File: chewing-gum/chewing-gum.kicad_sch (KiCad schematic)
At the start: 19 parts, among them IC9 INA212AIDCKR, J15 Conn_02x01, J23 Conn_02x01, J28 Conn_01x03, J36 Conn_01x01_Socket, J42 Conn_Coaxial, J78 Conn_01x03, U21 TLV75801PDBV

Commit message: First version of the chewing gum Vdc
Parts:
- removed J36: Conn_01x01_Socket, Connector:Banana_Jack_1Pin, symbol Connector:Conn_01x01_Socket
- removed TPVBLD3: TestPoint, TestPoint:TestPoint_Plated_Hole_D2.0mm, symbol Connector:TestPoint
- added J10, J9: Conn_01x04, Connector_PinHeader_1.27mm:PinHeader_1x04_P1.27mm_Vertical, symbol Connector_Generic:Conn_01x04
- added J11: Conn_02x01, Connector_PinHeader_2.54mm:PinHeader_1x02_P2.54mm_Vertical, symbol Connector_Generic:Conn_02x01
- added J6: Conn_01x01_Socket, Connector:Banana_Jack_1Pin, symbol Connector:Conn_01x01_Socket
- added J7, J8: Conn_01x06, Connector_PinHeader_1.27mm:PinHeader_1x06_P1.27mm_Vertical, symbol Connector_Generic:Conn_01x06
- added R4: 48.7k, Resistor_SMD:R_0603_1608Metric, symbol Device:R_Small
- renumbered C57 to C1, C41 to C2, C58 to C3, IC9 to IC1, J28 to J1, J42 to J2, J78 to J3, J15 to J4, J23 to J5, R49 to R1, R34 to R2, R41 to R3, R42 to R5, R20 to R6, RV5 to RV1, U21 to U1
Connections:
- net 3V3_LDO is gone; now on net 3V3: J1.1 (Pin_1)
- net GND: now also J10.1 (Pin_1), J10.2 (Pin_2), J7.3 (Pin_3), J8.3 (Pin_3), J9.1 (Pin_1), J9.2 (Pin_2), R4.2
- net REF_INA: now also J8.6 (Pin_6)
- net V_ldo_feedback: now reaches J3.2 (Pin_2), R3.1, U1.4 (FB)
- net V_ldo_feedback: now also J7.1 (Pin_1)
- net +3.3VA renamed 3V3
- net 3V3: now also J8.5 (Pin_5)
- net DAC4 renamed DAC_ctrl
- net DAC_ctrl: now also J7.2 (Pin_2), R4.1
- net EN_VBLADE3 renamed LDO_EN_EXT
- net LDO_EN_EXT: now also J8.1 (Pin_1)
- net V_B3_INA renamed V_out_test_p
- net V_out_test_p: now also J11.2 (Pin_2)
- net V_B3_load renamed V_out
- net V_out: now also J6.1 (Pin_1), J9.3 (Pin_3), J9.4 (Pin_4)
- net V_B3_load_n renamed V_out_test_n
- net V_out_test_n: now also J11.1 (Pin_1)
- net V_B3_o renamed V_diff_ampl_out
- net V_diff_ampl_out: now also J10.3 (Pin_3)
- net vblade3_ldo renamed V_ldo_out
- net V_ldo_out: now also J7.6 (Pin_6)
- no-connect marks 1 -> 0
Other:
- note added: "1-2: LDO on 2-3: External enable open: LDO off"
- note added: "1-2: Trimmer Control 2-3: DAC Control"
- note removed: "1-2: LDO on 2-3: I2C enables LDO open: LDO off"
- note removed: "1-2: Potentiometer Control 2-3: DAC Control"
- moved on the sheet: C2, IC1, J1, J2, J3, J4, J5, R6

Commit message: Finished ADC/DAC board
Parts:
- removed J6: Conn_01x01_Socket, Connector:Banana_Jack_1Pin, symbol Connector:Conn_01x01_Socket
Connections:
- net GND: now also J8.4 (Pin_4); no longer J8.3 (Pin_3)
- net V_diff_ampl_out: now also J10.4 (Pin_4); no longer J10.3 (Pin_3)
- no-connect marks 0 -> 5
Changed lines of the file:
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@@
-	)
-	(junction
-		(at 142.24 55.88)
-		(diameter 0)
-		(color 0 0 0 0)
 	)
 	(junction
@@
 		(color 0 0 0 0)
 	)
+	(no_connect
+		(at 116.84 147.32)
+	)
+	(no_connect
+		(at 143.51 173.99)
+	)
+	(no_connect
+		(at 149.86 142.24)
+	)
+	(no_connect
+		(at 149.86 139.7)
+	)
+	(no_connect
+		(at 116.84 144.78)
+	)
 	(wire
 		(pts
@@
 	(wire
 		(pts
-			(xy 142.24 173.99) (xy 144.78 173.99)
-		)
-		(stroke
-			(width 0)
-			(type default)
-		)
-	)
-	(wire
-		(pts
 			(xy 49.53 81.28) (xy 49.53 83.82)
 		)
@@
 	(wire
 		(pts
-			(xy 142.24 53.34) (xy 142.24 55.88)
-		)
-		(stroke
-			(width 0)
-			(type default)
-		)
-	)
-	(wire
-		(pts
 			(xy 67.31 170.18) (xy 87.63 170.18)
 		)
@@
 	(wire
 		(pts
-			(xy 152.4 53.34) (xy 142.24 53.34)
-		)
-		(stroke
-			(width 0)
-			(type default)
-		)
-	)
-	(wire
-		(pts
 			(xy 110.49 168.91) (xy 110.49 170.18)
 		)
@@
 	(wire
 		(pts
+			(xy 143.51 173.99) (xy 144.78 173.99)
+		)
+		(stroke
+			(width 0)
+			(type default)
+		)
+	)
+	(wire
+		(pts
 			(xy 103.505 96.52) (xy 93.98 96.52)
 		)
@@
 		(pts
 			(xy 116.84 91.44) (xy 116.84 93.98)
+		)
+		(stroke
+			(width 0)
+			(type default)
+		)
+	)
+	(wire
+		(pts
+			(xy 143.51 176.53) (xy 144.78 176.53)
 		)
 		(stroke
@@
 		)
 	)
-	(label "GND"
-		(at 149.86 142.24 180)
-		(effects
-			(font
-				(size 1.27 1.27)
-			)
-			(justify right bottom)
-		)
-	)
 	(label "3V3"
 		(at 53.34 83.82 180)
@@
 	)
 	(label "V_diff_ampl_out"
-		(at 142.24 173.99 180)
+		(at 143.51 176.53 180)
 		(effects
 			(font
@@
 			)
 			(justify left bottom)
+		)
+	)
+	(label "GND"
+		(at 149.86 144.78 180)
+		(effects
+			(font
+				(size 1.27 1.27)
+			)
+			(justify right bottom)
 		)
 	)
@@
 					(unit 1)
 				)
-			)
-		)
-	)
-	(symbol
-		(lib_id "Connector:Conn_01x01_Socket")
-		(at 157.48 53.34 0)
-		(unit 1)
-		(exclude_from_sim no)
-		(in_bom yes)
-		(on_board yes)
-		(dnp no)
-		(property "Reference" "J6"
-			(at 157.48 57.15 90)
-			(effects
-				(font
-					(size 1.27 1.27)
-				)
-				(justify left)
-			)
-		)
-		(property "Value" "Conn_01x01_Socket"
-			(at 165.735 53.34 0)
-			(effects
-				(font
-					(size 1.27 1.27)
-				)
-				(justify left)
-				(hide yes)
-			)
-		)
-		(property "Footprint" "Connector:Banana_Jack_1Pin"
-			(at 157.48 53.34 0)
-			(effects
-				(font
-					(size 1.27 1.27)
-				)
-				(hide yes)
-			)
-		)
-		(property "Datasheet" "~"
-			(at 157.48 53.34 0)
-			(effects
-				(font
-					(size 1.27 1.27)
-				)
-				(hide yes)
-			)
-		)
-		(property "Description" ""
-			(at 157.48 53.34 0)
-			(effects
-				(font
-					(size 1.27 1.27)
-				)
-				(hide yes)
-			)
-		)
-		(pin "1"
-		)
-		(instances
-			(project "chewing-gum"
-				(path "/c199eb24-c33c-4d87-8bb8-b17a18fed446"
-					(reference "J6")
-					(unit 1)
-				)

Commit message: Before re-organizing the main board
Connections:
- net Vpm is gone; now on net 5V: C1.1, U1.1 (IN)
- net 5V: now reaches J8.2 (Pin_2)
- net 5V: now also J8.3 (Pin_3)
- no-connect marks 5 -> 3
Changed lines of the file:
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@@
-	)
-	(no_connect
-		(at 149.86 142.24)
-	)
-	(no_connect
-		(at 149.86 139.7)
 	)
 	(no_connect
@@
 		)
 	)
+	(label "5V"
+		(at 149.86 139.7 180)
+		(effects
+			(font
+				(size 1.27 1.27)
+			)
+			(justify right bottom)
+		)
+	)
 	(label "V_diff_ampl_out"
 		(at 68.58 170.18 0)
@@
 		)
 	)
-	(label "Vpm"
+	(label "5V"
 		(at 33.02 91.44 0)
 		(effects
@@
 		)
 	)
+	(label "5V"
+		(at 149.86 142.24 180)
+		(effects
+			(font
+				(size 1.27 1.27)
+			)
+			(justify right bottom)
+		)
+	)

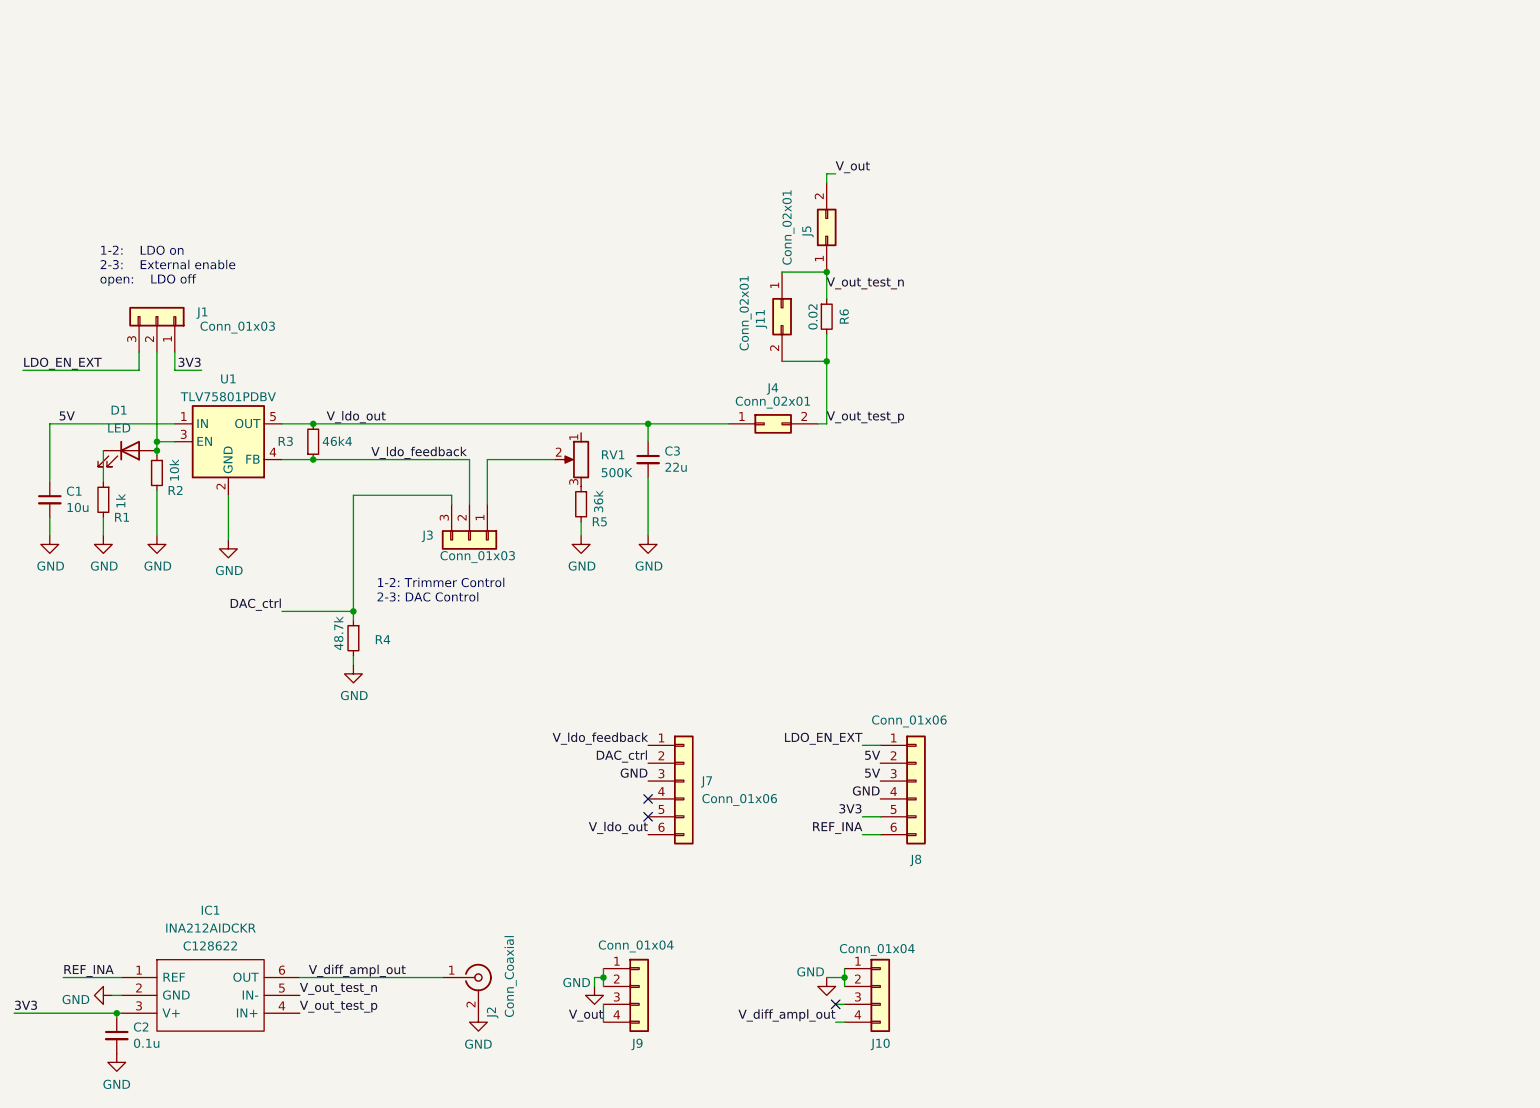
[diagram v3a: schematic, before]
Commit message: WIP: added i2c expanders and re-structuring i2c distributino
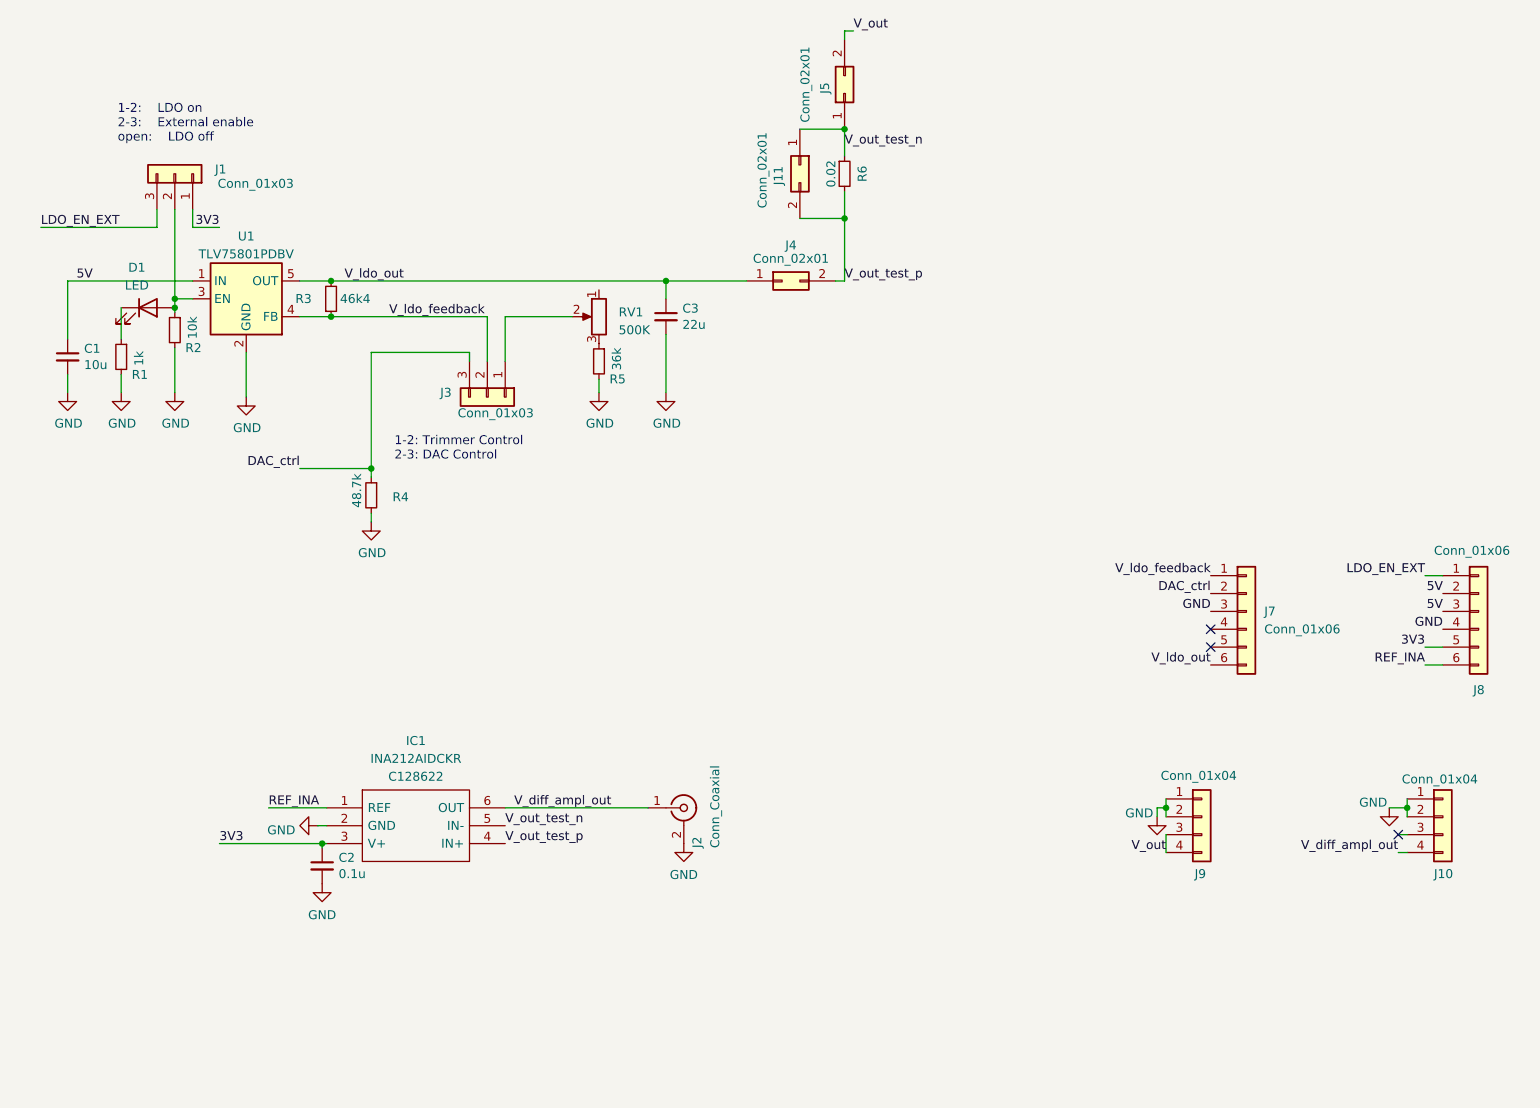
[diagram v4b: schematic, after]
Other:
- moved on the sheet: C1, C2, C3, D1, IC1, J1, J10, J11, J2, J3, J4, J5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
